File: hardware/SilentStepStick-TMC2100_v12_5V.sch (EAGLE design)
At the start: 30 parts, among them IC1 TMC2100-LA, X1 PASSER-07, X2 PASSER-07

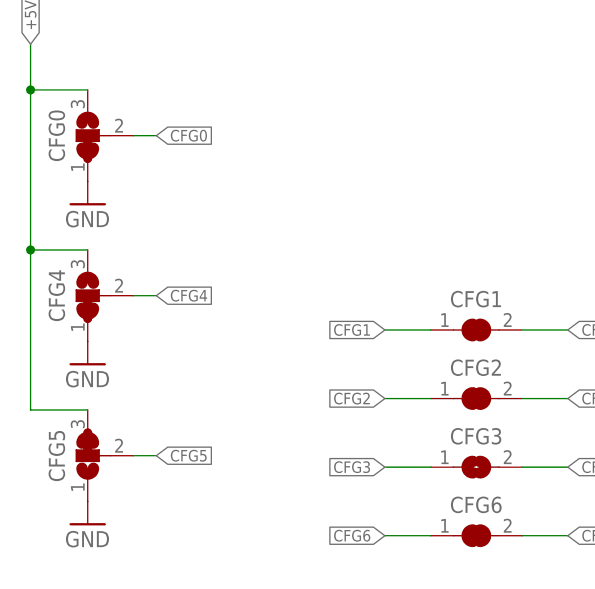
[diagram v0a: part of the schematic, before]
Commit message: updated schematics
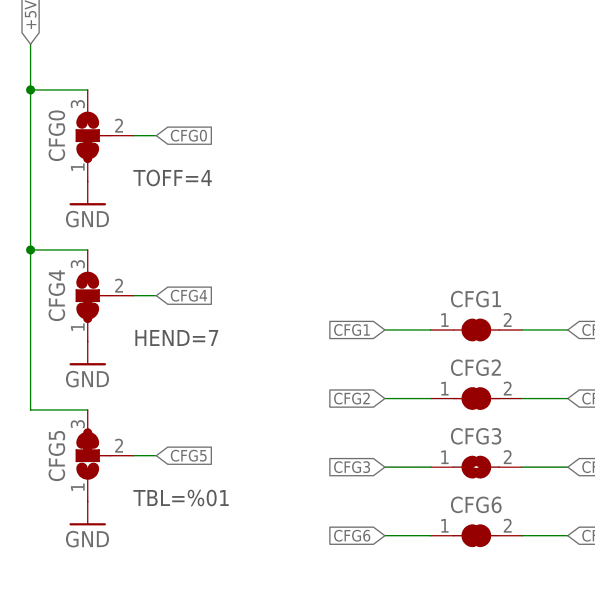
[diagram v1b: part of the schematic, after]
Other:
- note added: "HEND=7"
- note added: "TBL=%01"
- note added: "TOFF=4"
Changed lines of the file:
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@@
 <?xml version="1.0" encoding="utf-8"?>
 <!DOCTYPE eagle SYSTEM "eagle.dtd">
-<eagle version="7.6.0">
+<eagle version="7.7.0">
 <drawing>
 <settings>
@@
 <setting verticaltext="up"/>
 </settings>
-<grid distance="0.1" unitdist="inch" unit="inch" style="lines" multiple="1" display="no" altdistance="0.01" altunitdist="inch" altunit="inch"/>
+<grid distance="0.05" unitdist="inch" unit="inch" style="lines" multiple="1" display="yes" altdistance="0.025" altunitdist="inch" altunit="inch"/>
 <layers>
 <layer number="1" name="Top" color="4" fill="1" visible="no" active="no"/>
@@
 <wire x1="59.055" y1="24.13" x2="60.325" y2="24.13" width="1.016" layer="94"/>
 <wire x1="16.51" y1="50.8" x2="16.51" y2="53.34" width="1.016" layer="94"/>
+<text x="21.59" y="49.53" size="1.778" layer="97" font="vector" ratio="10" align="top-left">TOFF=4</text>
+<text x="21.59" y="31.75" size="1.778" layer="97" font="vector" ratio="10" align="top-left">HEND=7</text>
+<text x="21.59" y="13.97" size="1.778" layer="97" font="vector" ratio="10" align="top-left">TBL=%01</text>
 </plain>
 <instances>

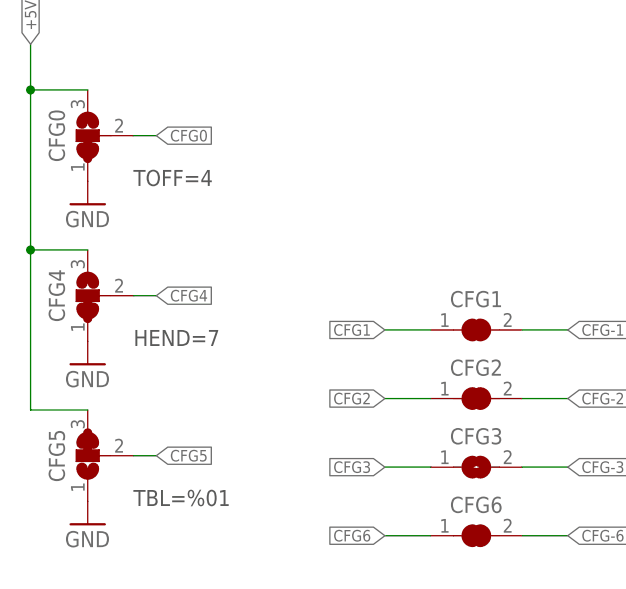
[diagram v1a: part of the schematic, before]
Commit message: updated schematics
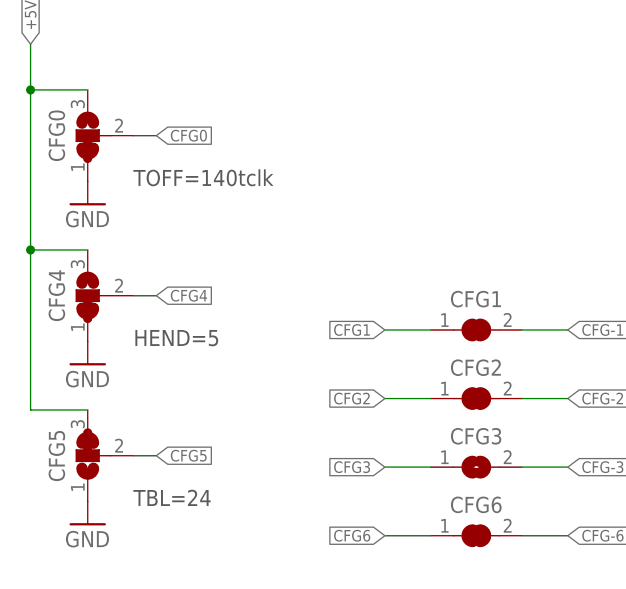
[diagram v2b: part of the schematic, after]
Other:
- note added: "HEND=5"
- note added: "TBL=24"
- note added: "TOFF=140tclk"
- note removed: "HEND=7"
- note removed: "TBL=%01"
- note removed: "TOFF=4"
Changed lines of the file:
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@@
 <setting verticaltext="up"/>
 </settings>
-<grid distance="0.05" unitdist="inch" unit="inch" style="lines" multiple="1" display="yes" altdistance="0.025" altunitdist="inch" altunit="inch"/>
+<grid distance="0.1" unitdist="inch" unit="inch" style="lines" multiple="1" display="no" altdistance="0.01" altunitdist="inch" altunit="inch"/>
 <layers>
 <layer number="1" name="Top" color="4" fill="1" visible="no" active="no"/>
@@
 <wire x1="59.055" y1="24.13" x2="60.325" y2="24.13" width="1.016" layer="94"/>
 <wire x1="16.51" y1="50.8" x2="16.51" y2="53.34" width="1.016" layer="94"/>
-<text x="21.59" y="49.53" size="1.778" layer="97" font="vector" ratio="10" align="top-left">TOFF=4</text>
-<text x="21.59" y="31.75" size="1.778" layer="97" font="vector" ratio="10" align="top-left">HEND=7</text>
-<text x="21.59" y="13.97" size="1.778" layer="97" font="vector" ratio="10" align="top-left">TBL=%01</text>
+<text x="21.59" y="49.53" size="1.778" layer="97" font="vector" ratio="10" align="top-left">TOFF=140tclk</text>
+<text x="21.59" y="31.75" size="1.778" layer="97" font="vector" ratio="10" align="top-left">HEND=5</text>
+<text x="21.59" y="13.97" size="1.778" layer="97" font="vector" ratio="10" align="top-left">TBL=24</text>
 </plain>
 <instances>
